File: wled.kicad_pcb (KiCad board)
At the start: 2 copper layers, 61.5 x 28.4 mm, 19 parts, among them J1 PROGRAM_HEADER, J2 LED0, J3 QWIIC, J4 POWER, Q1 S8050, Q2 S8050, U1 ESP-12F, U2 AMS1117-3.3

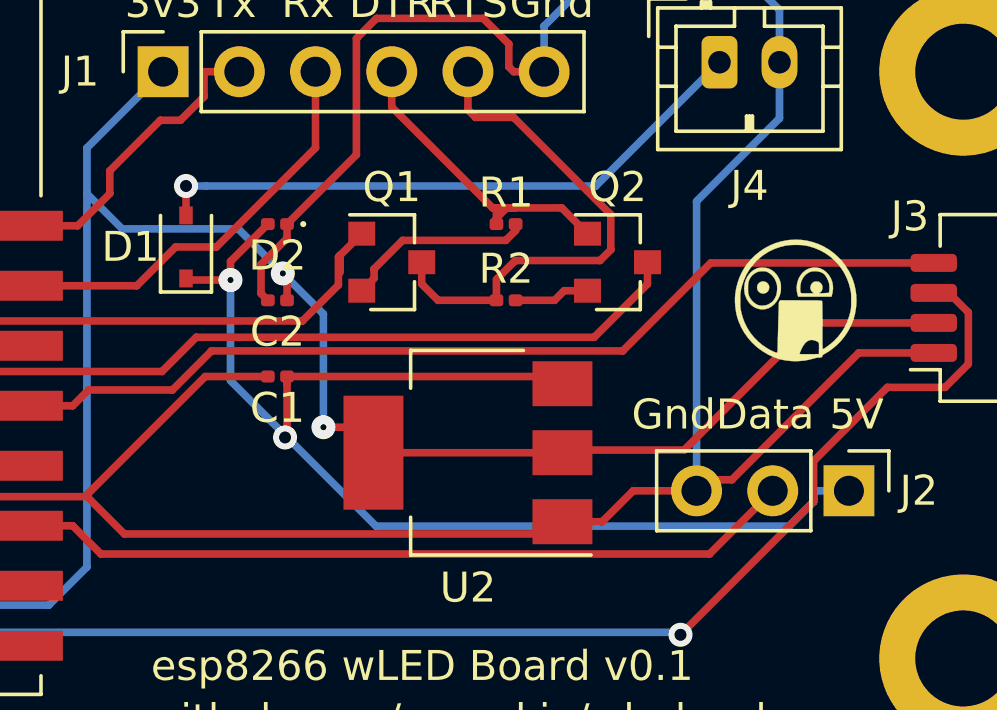
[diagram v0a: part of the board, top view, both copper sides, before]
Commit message: fix vias per JLCPCB email
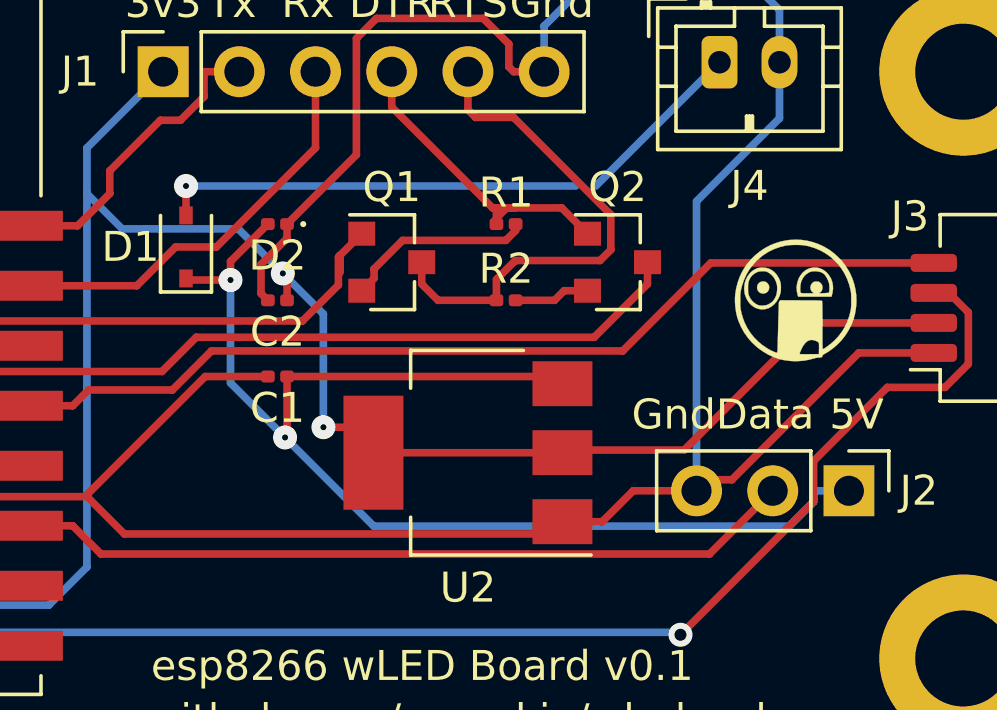
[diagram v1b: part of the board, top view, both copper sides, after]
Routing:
- net VIN: track 20.5 -> 19.8 mm

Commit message: update and resubmit
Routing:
- net VIN: track 19.8 -> 20.5 mm
- net VDD3V3: track 72.7 -> 72.1 mm

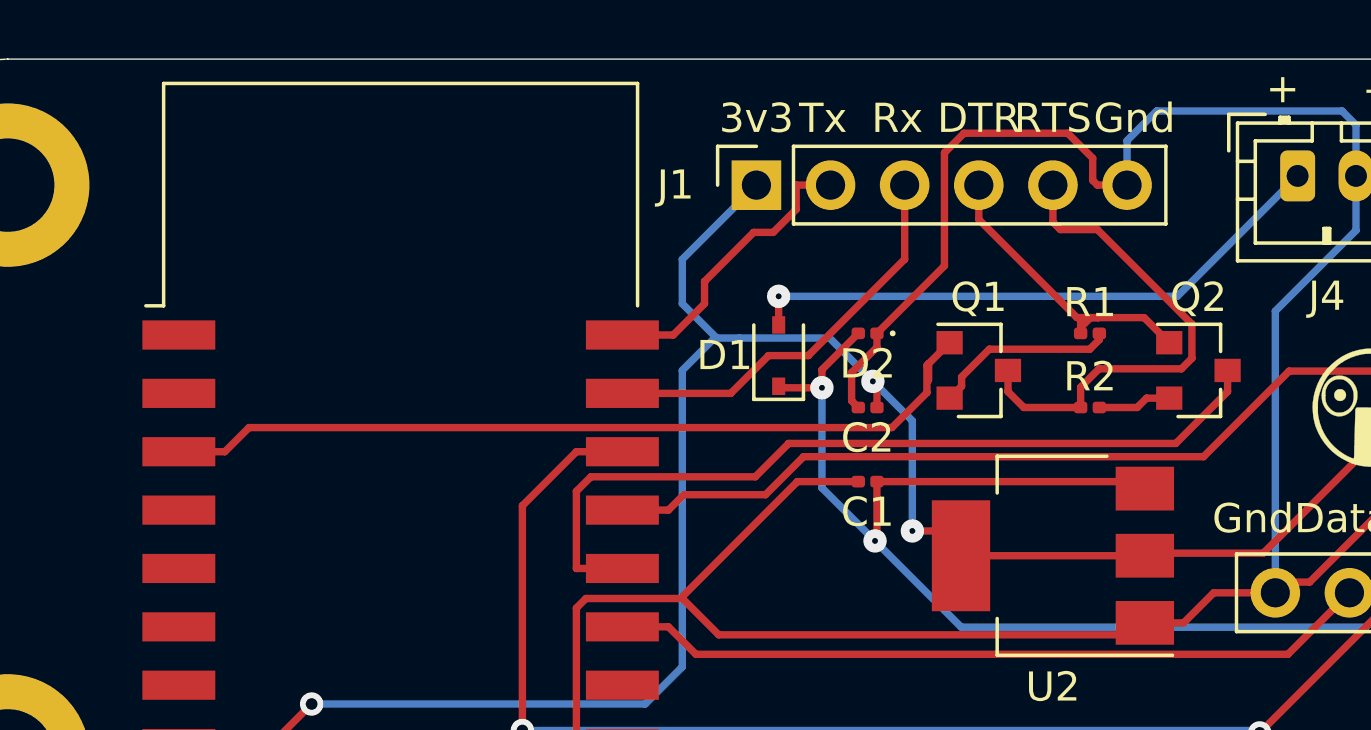
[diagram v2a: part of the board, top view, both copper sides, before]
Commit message: fix 0603 components
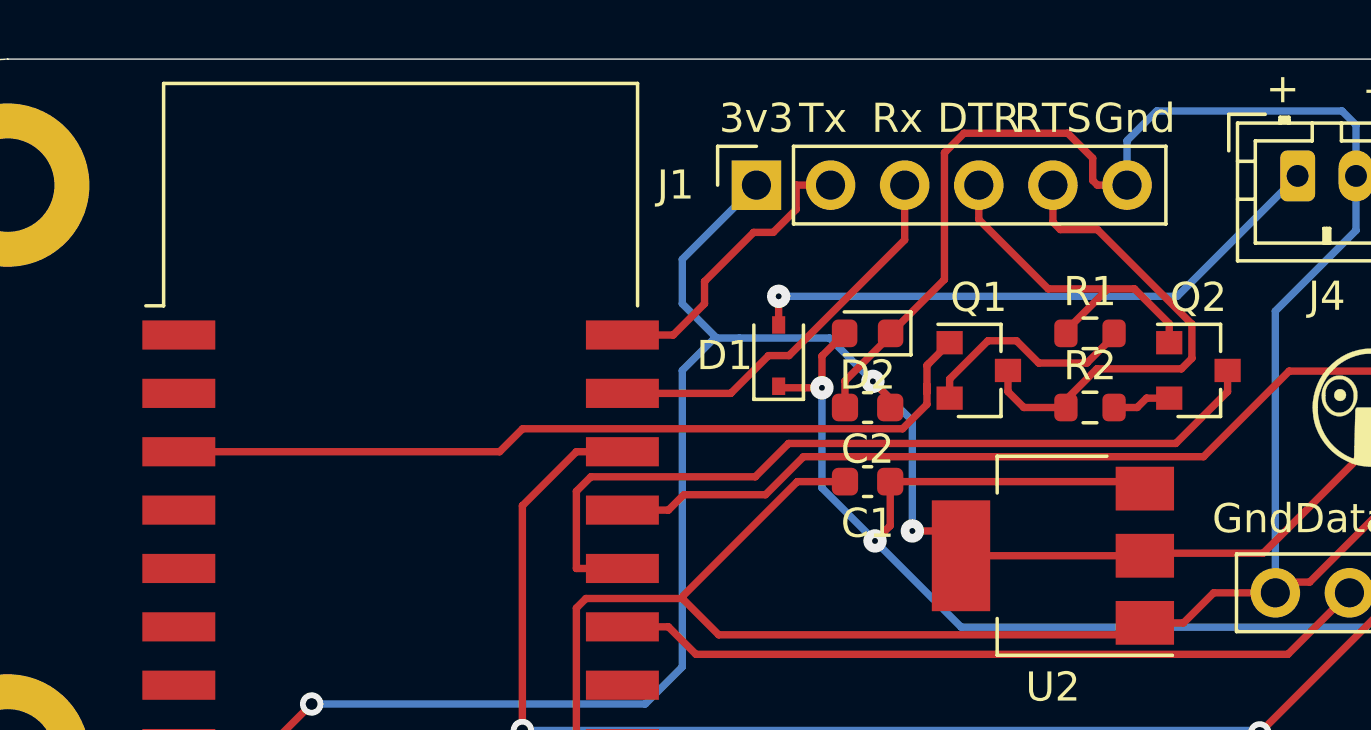
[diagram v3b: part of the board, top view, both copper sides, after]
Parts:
- C1, C2: footprint Capacitor_SMD:C_0201_0603Metric -> Capacitor_SMD:C_0603_1608Metric
- D2: footprint LED_SMD:LED_0201_0603Metric -> LED_SMD:LED_0603_1608Metric
- R1, R2: footprint Resistor_SMD:R_0201_0603Metric -> Resistor_SMD:R_0603_1608Metric
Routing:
- net Net-(Q1-Pad2): track 6.36 -> 7.66 mm
- net DTR: track 10.9 -> 12.0 mm
- net Net-(Q2-Pad2): track 2.53 -> 2.02 mm

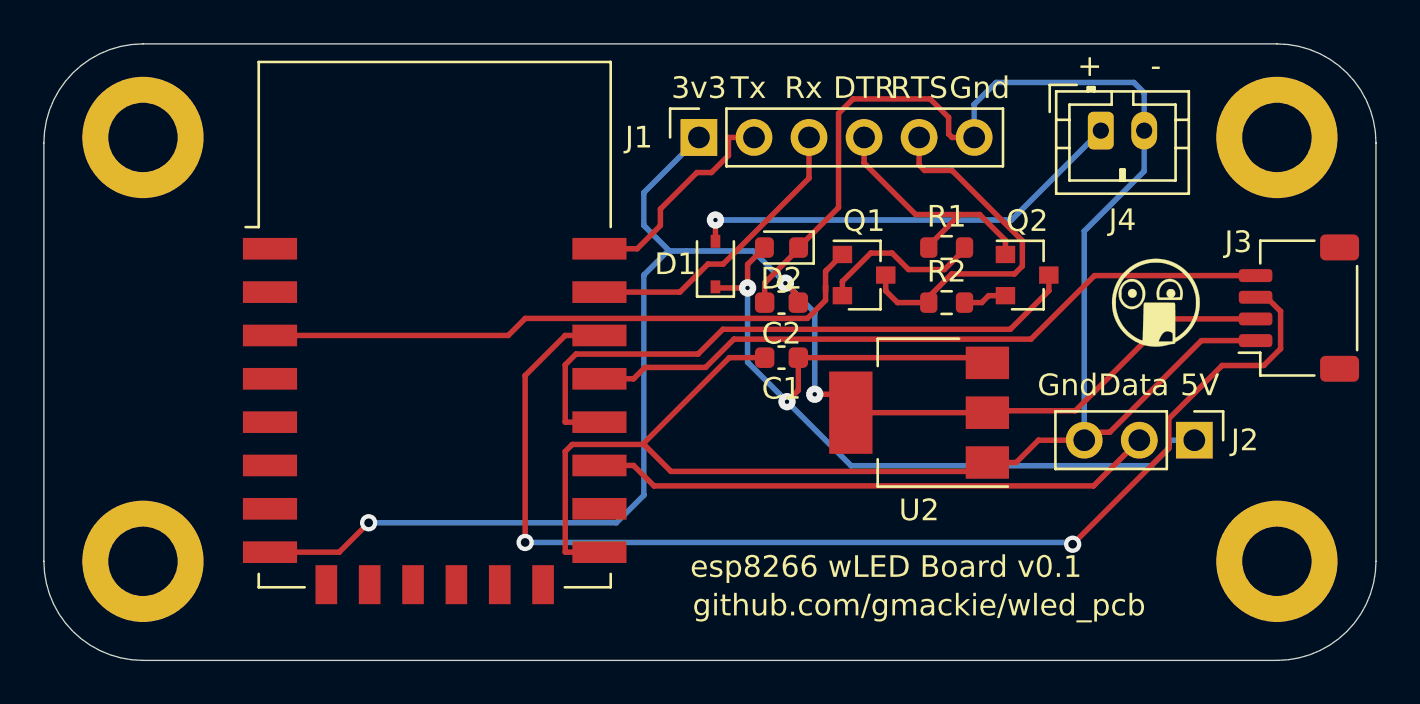
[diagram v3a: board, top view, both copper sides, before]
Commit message: updated parts/placements
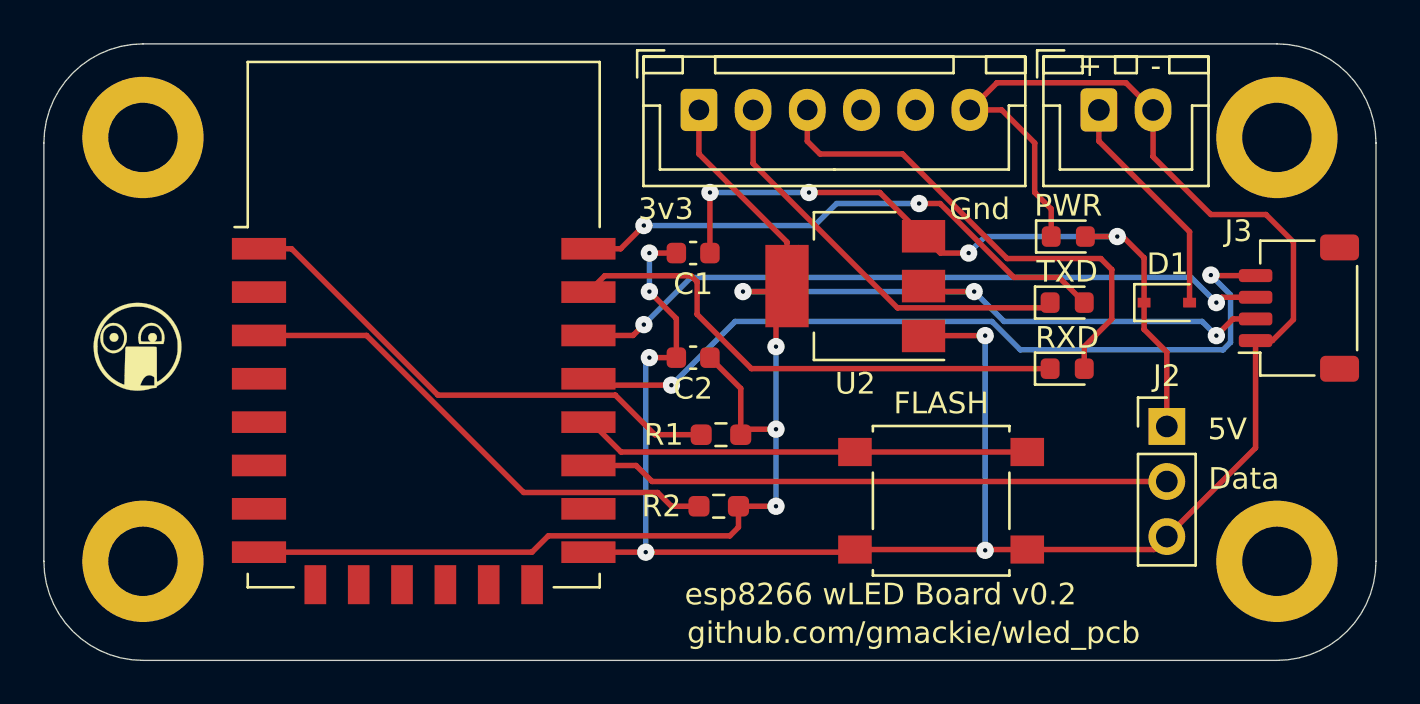
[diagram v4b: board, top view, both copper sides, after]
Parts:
- removed D2: LED, LED_SMD:LED_0603_1608Metric
- removed Q1, Q2: S8050, Package_TO_SOT_SMD:SOT-23
- added FLASH: FLASH, Button_Switch_SMD:SW_SPST_B3S-1000, F.Cu at (60.7, 43.4)
- added PWR: LED, LED_SMD:LED_0603_1608Metric, F.Cu at (66.6, 31.2)
- added RXD: LED, LED_SMD:LED_0603_1608Metric, F.Cu at (66.5, 37.3)
- added TXD: LED, LED_SMD:LED_0603_1608Metric, F.Cu at (66.5, 34.3)
- J1: footprint Connector_PinSocket_2.54mm:PinSocket_1x06_P2.54mm_Vertical -> Connector_JST:JST_XH_B6B-XH-A_1x06_P2.50mm_Vertical
- J4: footprint Connector_JST:JST_PH_B2B-PH-K_1x02_P2.00mm_Vertical -> Connector_JST:JST_XH_B2B-XH-A_1x02_P2.50mm_Vertical
- R1, R2: value 12k -> 10K; footprint Resistor_SMD:R_0603_1608Metric -> Resistor_SMD:R_0603_1608Metric_Pad0.98x0.95mm_HandSolder
- moved G*** 47.0 mm to (23.6, 36.3)
- moved D1 20.9 mm to (71.1, 34.3), turned to 0 degrees
- moved R2 14.1 mm to (50.4, 43.7)
- moved R1 13.5 mm to (50.5, 40.4)
- moved U2 6.54 mm to (56.7, 33.5)
- moved C1 6.32 mm to (49.3, 32.0)
- moved C2 4.80 mm to (49.3, 36.8)
- moved J2 1.42 mm to (71.1, 40.0), turned to 0 degrees
- moved J1 1.27 mm to (49.5, 25.4), turned to 0 degrees
- moved J4 0.96 mm to (68.0, 25.4)
- moved U1 0.51 mm to (36.8, 35.3)
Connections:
- J1 pad 4: DTR -> (no net)
- J1 pad 5: RTS -> (no net)
- R1 pad 1: DTR -> Net-(R1-Pad1)
- R1 pad 2: Net-(Q1-Pad2) -> VDD3V3
- R2 pad 1: RTS -> Net-(R2-Pad1)
- R2 pad 2: Net-(Q2-Pad2) -> VDD3V3
- U1 pad 1: Net-(U1-Pad1) -> Net-(R1-Pad1)
- U1 pad 10: Net-(U1-Pad10) -> (no net)
- U1 pad 11: Net-(U1-Pad11) -> (no net)
- U1 pad 12: Net-(U1-Pad12) -> (no net)
- U1 pad 13: Net-(U1-Pad13) -> (no net)
- U1 pad 14: Net-(U1-Pad14) -> (no net)
- U1 pad 16: Net-(U1-Pad16) -> (no net)
- U1 pad 18: GPIO0 -> Net-(SW2-Pad1)
- U1 pad 2: Net-(U1-Pad2) -> (no net)
- U1 pad 21: RXD -> Net-(D4-Pad1)
- U1 pad 22: TXD -> Net-(D3-Pad2)
- U1 pad 3: EN -> Net-(R2-Pad1)
- U1 pad 4: Net-(U1-Pad4) -> (no net)
- U1 pad 5: Net-(U1-Pad5) -> (no net)
- U1 pad 6: Net-(U1-Pad6) -> (no net)
- U1 pad 7: Net-(U1-Pad7) -> (no net)
- U1 pad 9: Net-(U1-Pad9) -> (no net)
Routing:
- net EN: track 29.0 -> 0.00 mm
- net GPIO0: track 28.7 -> 0.00 mm
- net Net-(D3-Pad2): track 0.00 -> 26.2 mm, vias 0 -> 2
- net Net-(D4-Pad1): track 0.00 -> 24.3 mm
- net Net-(R1-Pad1): track 0.00 -> 24.0 mm
- net Net-(R2-Pad1): track 0.00 -> 23.6 mm
- net SDA: track 54.3 -> 32.5 mm
- net Net-(SW2-Pad1): track 0.00 -> 20.8 mm
- net RTS: track 16.8 -> 0.00 mm
- net DTR: track 12.0 -> 0.00 mm
- net VDD3V3: track 72.5 -> 82.8 mm, vias 3 -> 6
- net VIN: track 20.5 -> 10.6 mm, vias 1 -> 0
- net RXD: track 13.7 -> 23.0 mm
- net TXD: track 10.3 -> 19.0 mm
- net GND: track 94.0 -> 101.7 mm, vias 0 -> 6
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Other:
- board text added: "esp8266 wLED Board v0.2"
- board text removed: "DTR"
- board text removed: "RTS"
- board text removed: "Rx"
- board text removed: "Tx"
- board text removed: "esp8266 wLED Board v0.1"

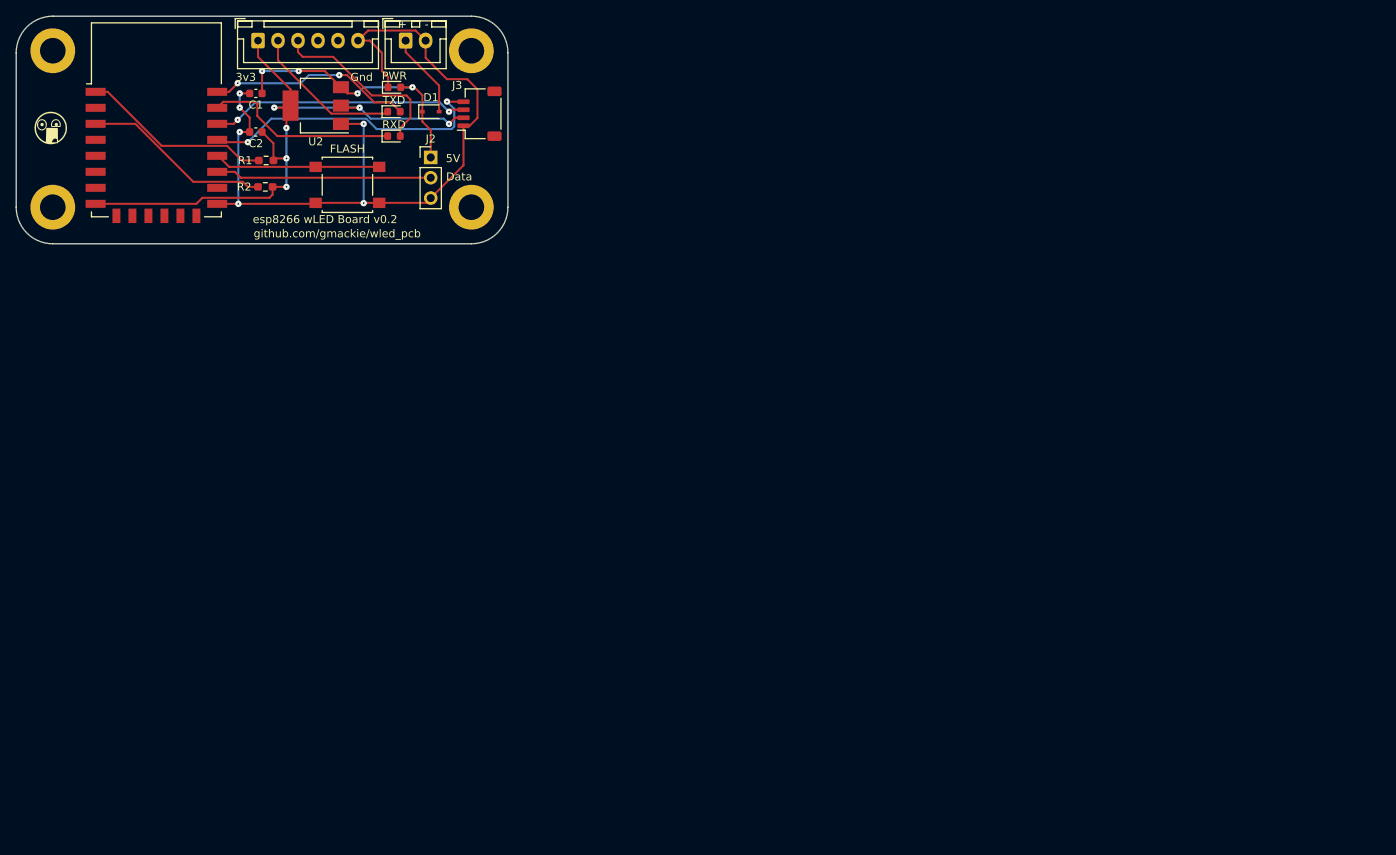
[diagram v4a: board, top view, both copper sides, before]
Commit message: updated pcb origin... still not aligned properly for jlc
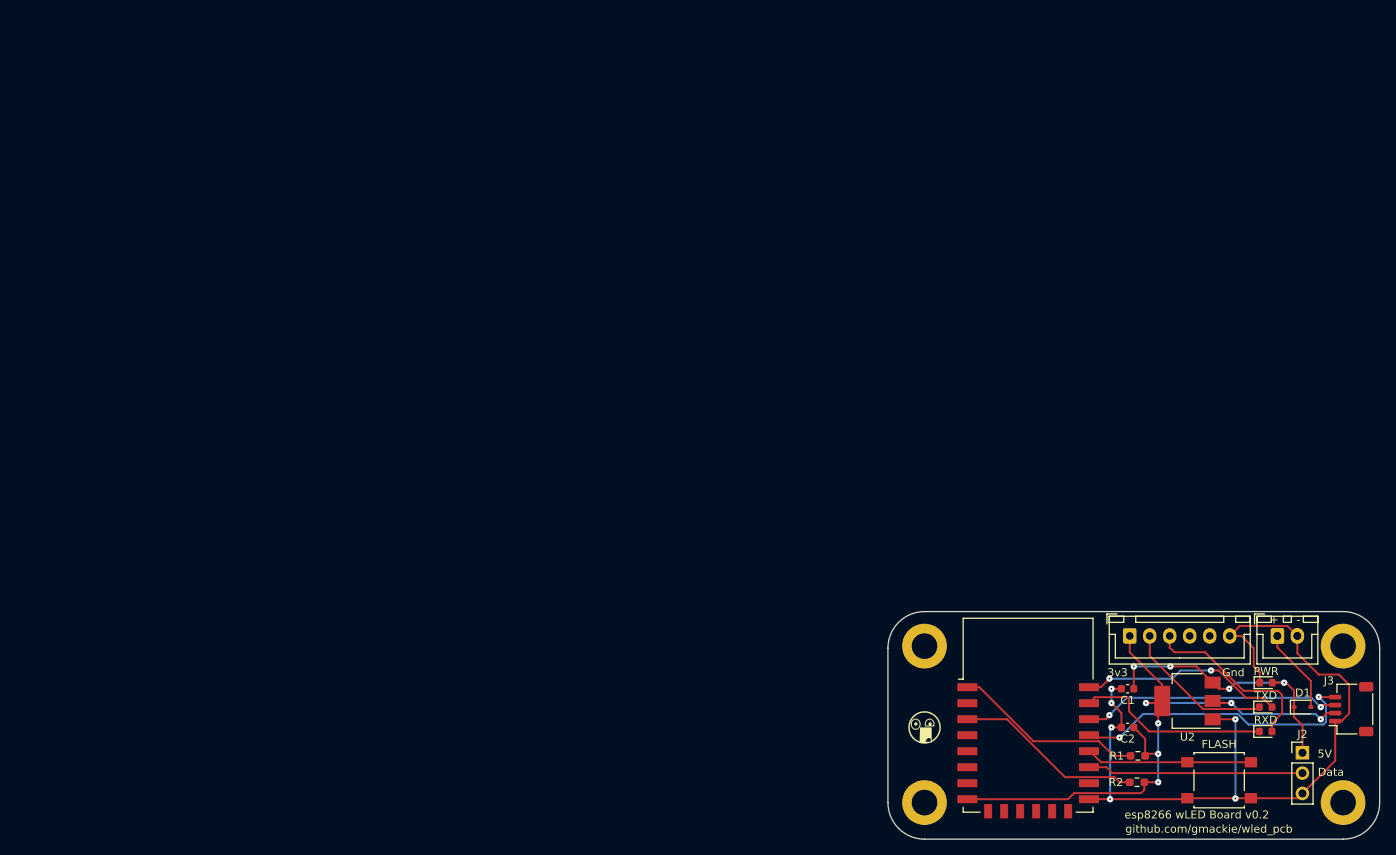
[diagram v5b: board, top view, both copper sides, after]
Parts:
- moved G*** 132.5 mm to (132.8, 111.3)
- moved C1 132.0 mm to (158.2, 106.4)
- moved C2 132.0 mm to (158.2, 111.3)
- moved D1 132.0 mm to (180.1, 108.7)
- moved H1 132.0 mm to (132.8, 120.7)
- moved H2 132.0 mm to (132.8, 101.1)
- moved J1 132.0 mm to (158.5, 99.8)
- moved J2 132.0 mm to (180.1, 114.4)
- moved PWR 132.0 mm to (175.5, 105.7)
- moved R1 132.0 mm to (159.5, 114.8)
- moved R2 132.0 mm to (159.4, 118.1)
- moved U2 132.0 mm to (165.7, 108.0)
- moved FLASH 132.0 mm to (169.7, 117.9)
- moved H3 132.0 mm to (185.2, 101.1)
- moved H4 132.0 mm to (185.2, 120.7)
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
